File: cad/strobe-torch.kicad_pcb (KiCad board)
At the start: 2 copper layers, 81 x 34 mm, 32 parts, among them SW1 50Hz, SW2 60Hz, SW3 300Hz, U1 ATTINY25V-10SU, Y1 4.9152MHz

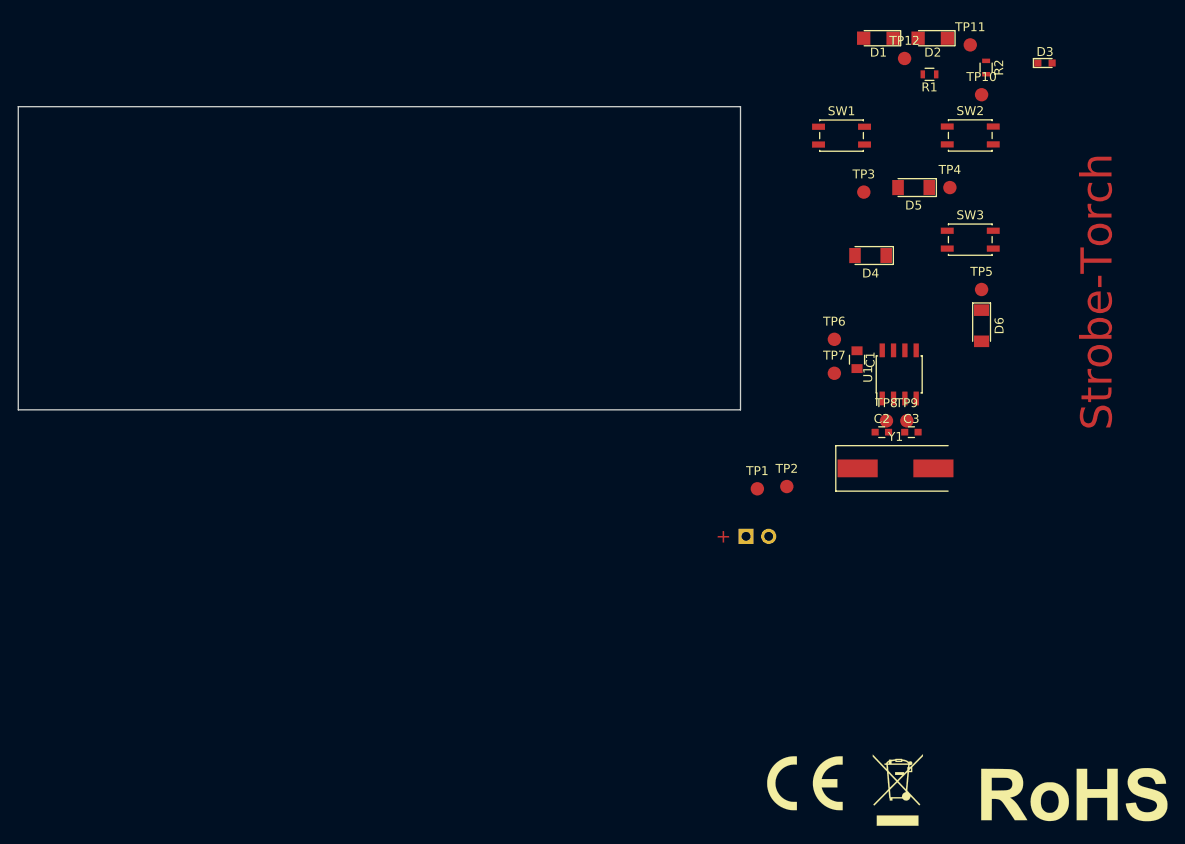
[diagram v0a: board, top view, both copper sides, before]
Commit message: Updated schematic (Output MOSFET and change to Shottky diodes, changed pinning to optimize layout)
Created footprints for Teko case and side emitting LEDs

Initial pcb layout
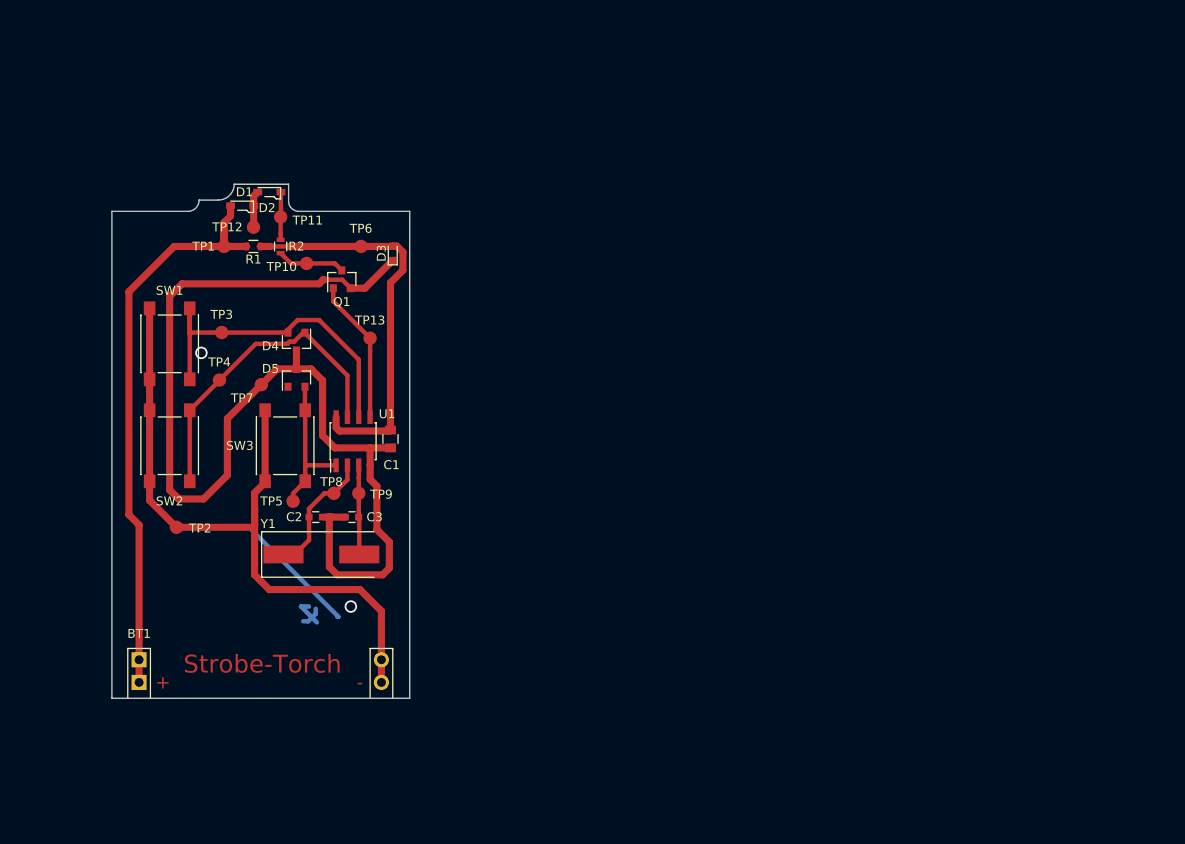
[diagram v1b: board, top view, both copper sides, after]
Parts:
- removed D6: 1N4148, Diodes_SMD:D_MiniMELF
- removed REF***: RoHS-Logo_6mm_SilkScreen, Symbols:RoHS-Logo_6mm_SilkScreen
- removed REF***: CE-Logo_8.5x6mm_SilkScreen, Symbols:CE-Logo_8.5x6mm_SilkScreen
- removed REF***: WEEE-Logo_5.6x8mm_SilkScreen, Symbols:WEEE-Logo_5.6x8mm_SilkScreen
- added Q1: BSS138, TO_SOT_Packages_SMD:SOT-23, F.Cu at (156.1, 78.4)
- added TP13: PWMout, Measurement_Points:Measurement_Point_Round-SMD-Pad_Small, F.Cu at (159.3, 85.0)
- BT1: footprint Pin_Headers:Pin_Header_Straight_1x02_Pitch2.54mm -> Battery_Holder:Teko_1112x_battery_compartment; moved to F.Cu
- D1, D2: footprint LEDs:LED_1206 -> LEDs_Side_Emitting:LED_215
- D4, D5: value 1N4148 -> BAT54A; footprint Diodes_SMD:D_MiniMELF -> TO_SOT_Packages_SMD:SOT-23
- R1: value 1k5 -> 1k8
- R2: value 270 -> 150
- SW1, SW2, SW3: footprint Buttons_Switches_SMD:SW_SPST_EVQP2 -> Buttons_Switches_SMD:SW_SPST_PTS645
- TP10: value PWMout -> Udrain
- moved SW2 96.3 mm to (136.8, 97.0), turned to 90 degrees
- moved TP4 84.7 mm to (142.4, 89.7)
- moved R2 81.6 mm to (149.2, 74.7)
- moved TP5 80.8 mm to (150.6, 103.3)
- moved SW3 80.2 mm to (149.7, 97.0), turned to 90 degrees
- moved TP11 79.7 mm to (149.2, 71.4)
- moved SW1 78.9 mm to (136.8, 85.6), turned to 90 degrees
- moved R1 78.2 mm to (146.2, 74.7)
- moved TP10 78.0 mm to (152.1, 76.6)
- moved D2 76.4 mm to (148.0, 68.6), turned to 0 degrees
- moved D3 76.2 mm to (161.8, 75.4), turned to 90 degrees
- moved TP12 75.4 mm to (146.2, 72.5)
- moved D1 73.8 mm to (144.9, 70.1), turned to 0 degrees
- moved TP3 73.7 mm to (142.6, 84.3)
- moved D5 72.4 mm to (151.0, 89.4), turned to 90 degrees
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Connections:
- D4 pad 2: GND -> Net-(D4-Pad2)
- D5 pad 1: Net-(D5-Pad1) -> (no net)
- D5 pad 2: GND -> Net-(D5-Pad2)
- R2 pad 2: Net-(R2-Pad2) -> Net-(Q1-Pad3)
- SW1 pad 2: Net-(D4-Pad1) -> Net-(D4-Pad2)
- SW2 pad 2: Net-(D5-Pad1) -> Net-(D4-Pad1)
- SW3 pad 2: Net-(D6-Pad1) -> Net-(D5-Pad2)
- TP10 pad 1: Net-(R2-Pad2) -> Net-(Q1-Pad3)
- TP3 pad 1: Net-(D4-Pad1) -> Net-(D4-Pad2)
- TP4 pad 1: Net-(D5-Pad1) -> Net-(D4-Pad1)
- TP5 pad 1: Net-(D6-Pad1) -> Net-(D5-Pad2)
- U1 pad 1: Net-(D6-Pad1) -> Net-(D5-Pad2)
- U1 pad 5: Net-(D5-Pad1) -> Net-(Q1-Pad1)
- U1 pad 6: Net-(R2-Pad2) -> Net-(D4-Pad2)
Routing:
- net GND: track 0.00 -> 124.1 mm
- net Net-(BT1-Pad2): track 0.00 -> 79.7 mm
- net +12V: track 0.00 -> 67.0 mm
- net VCC: track 0.00 -> 44.3 mm
- net Net-(D4-Pad2): track 0.00 -> 38.8 mm
- net Net-(D4-Pad1): track 0.00 -> 36.0 mm
- net (no net): track 0.00 -> 26.3 mm, vias 0 -> 2
- net Net-(D5-Pad2): track 0.00 -> 16.9 mm
- net Net-(Q1-Pad1): track 0.00 -> 16.2 mm
- net Net-(C2-Pad2): track 0.00 -> 14.3 mm
- net Net-(C3-Pad1): track 0.00 -> 10.1 mm
- net Net-(Q1-Pad3): track 0.00 -> 7.66 mm
- net Net-(D2-Pad1): track 0.00 -> 5.36 mm
- net Net-(D1-Pad1): track 0.00 -> 4.13 mm
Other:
- board size 81 x 34 mm -> 33.4 x 57.7 mm
- net class Default: trace_width 0.27 -> 0.5
- net class Led: trace_width 0.35 -> 0.8
- net class Power: trace_width 0.45 -> 0.8
- board text added: "-"

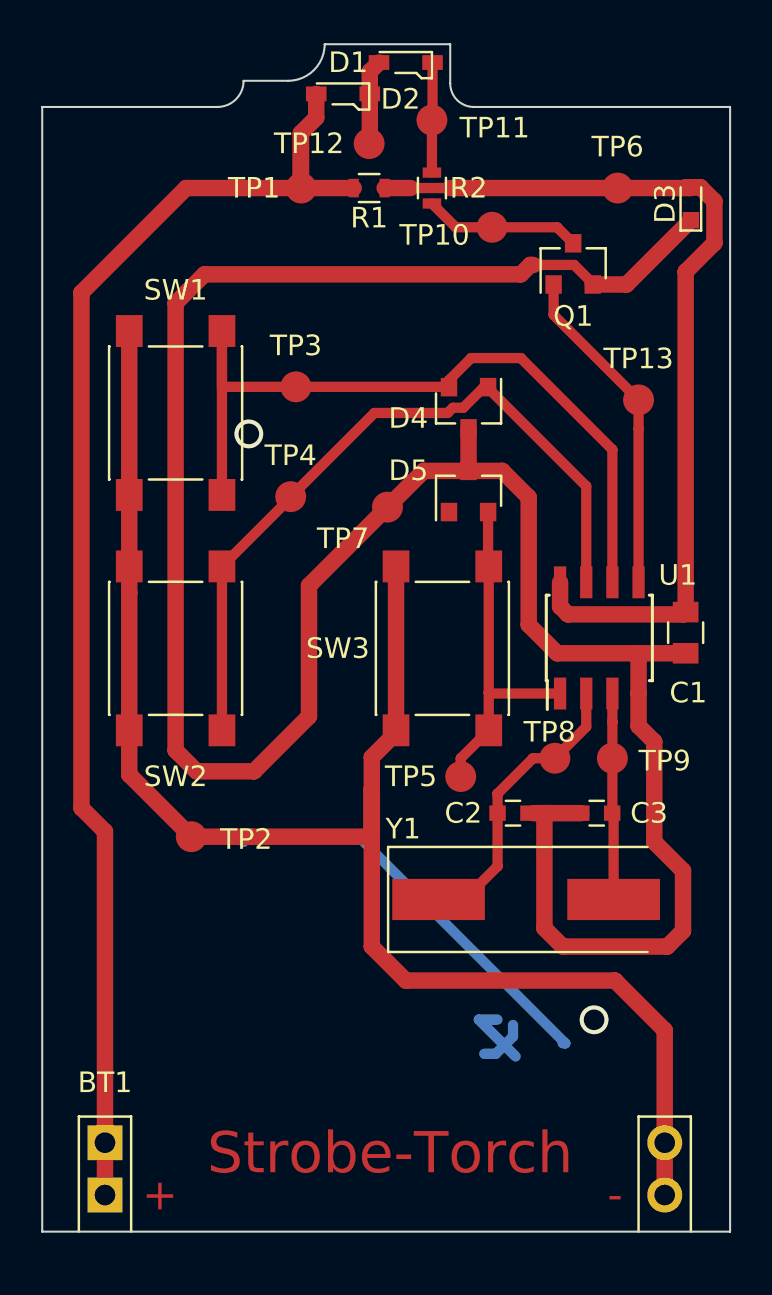
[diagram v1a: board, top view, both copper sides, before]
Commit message: Applied needed modifications after production of first samples.
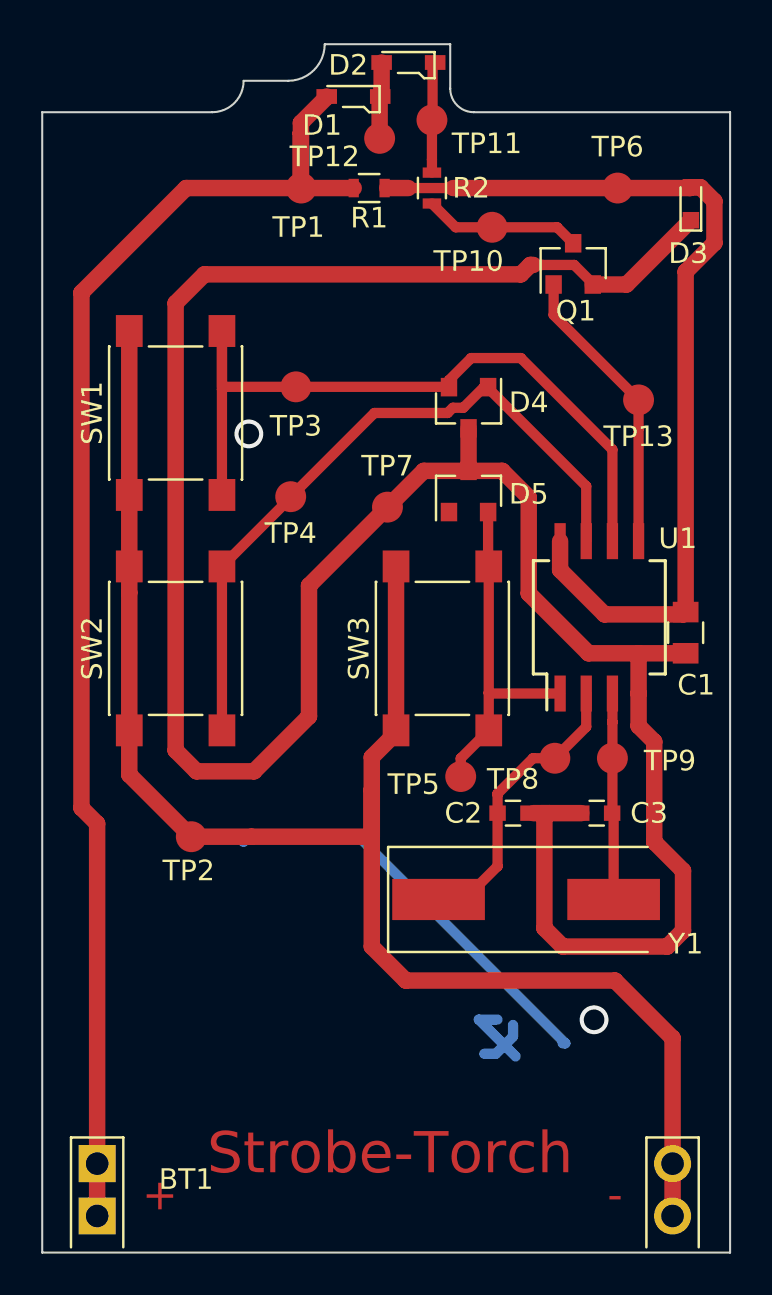
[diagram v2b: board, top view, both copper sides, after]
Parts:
- U1: footprint Housings_SOIC:SOIC-8_3.9x4.9mm_Pitch1.27mm -> Housings_SOIC:SO-8_5.3x6.2mm_Pitch1.27mm
- moved BT1 1.09 mm to (133.0, 122.0)
- moved U1 1.00 mm to (157.4, 95.5)
- moved TP12 0.57 mm to (146.7, 72.3)
- moved D1 0.52 mm to (145.4, 70.2)
- moved D2 0.13 mm to (148.1, 68.6)
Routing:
- net Net-(Q1-Pad1): track 16.2 -> 14.2 mm
- net Net-(D4-Pad2): track 38.8 -> 36.8 mm
- net Net-(D4-Pad1): track 36.0 -> 34.0 mm
- net Net-(BT1-Pad2): track 79.7 -> 80.9 mm
- net +12V: track 67.0 -> 68.0 mm
- net GND: track 124.1 -> 123.2 mm
- net VCC: track 44.3 -> 45.1 mm
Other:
- board size 33.4 x 57.7 mm -> 33.4 x 58.7 mm

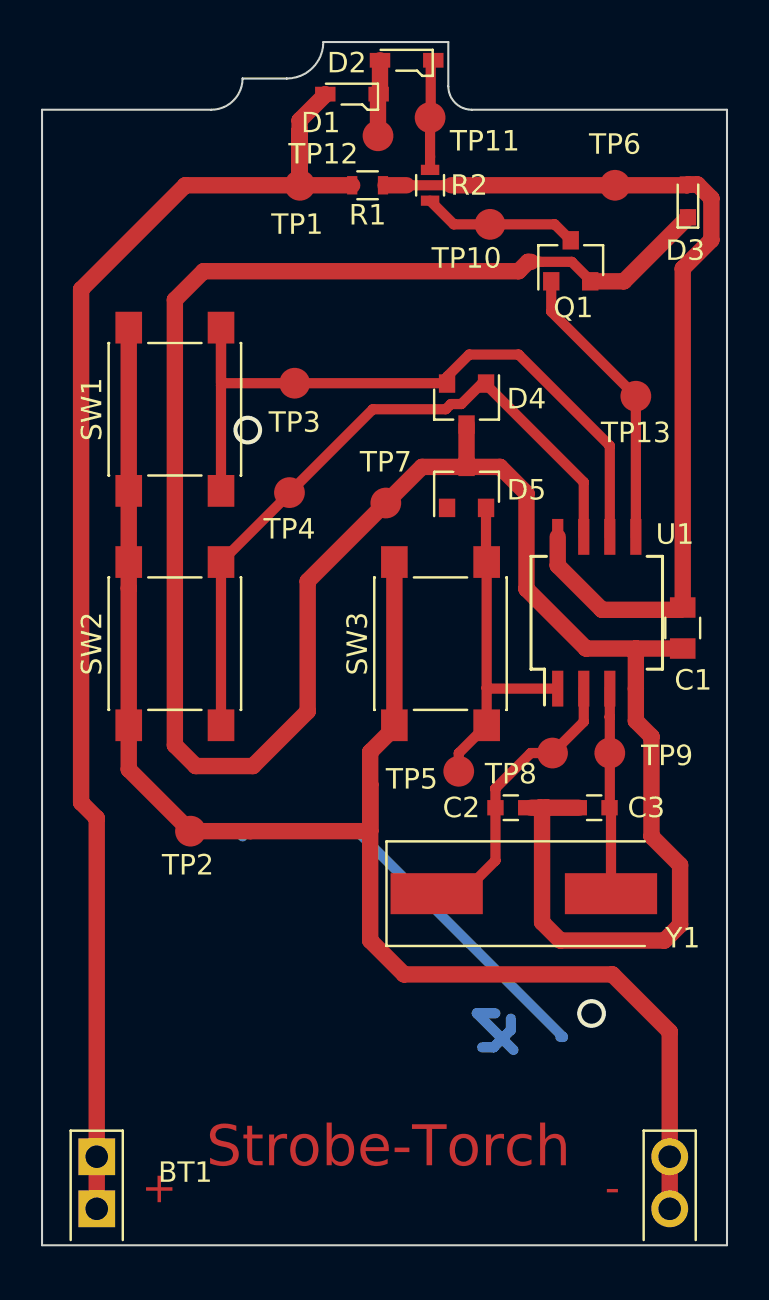
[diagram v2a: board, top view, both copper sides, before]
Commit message: Change footprint of button and upgrade to KiCad 8
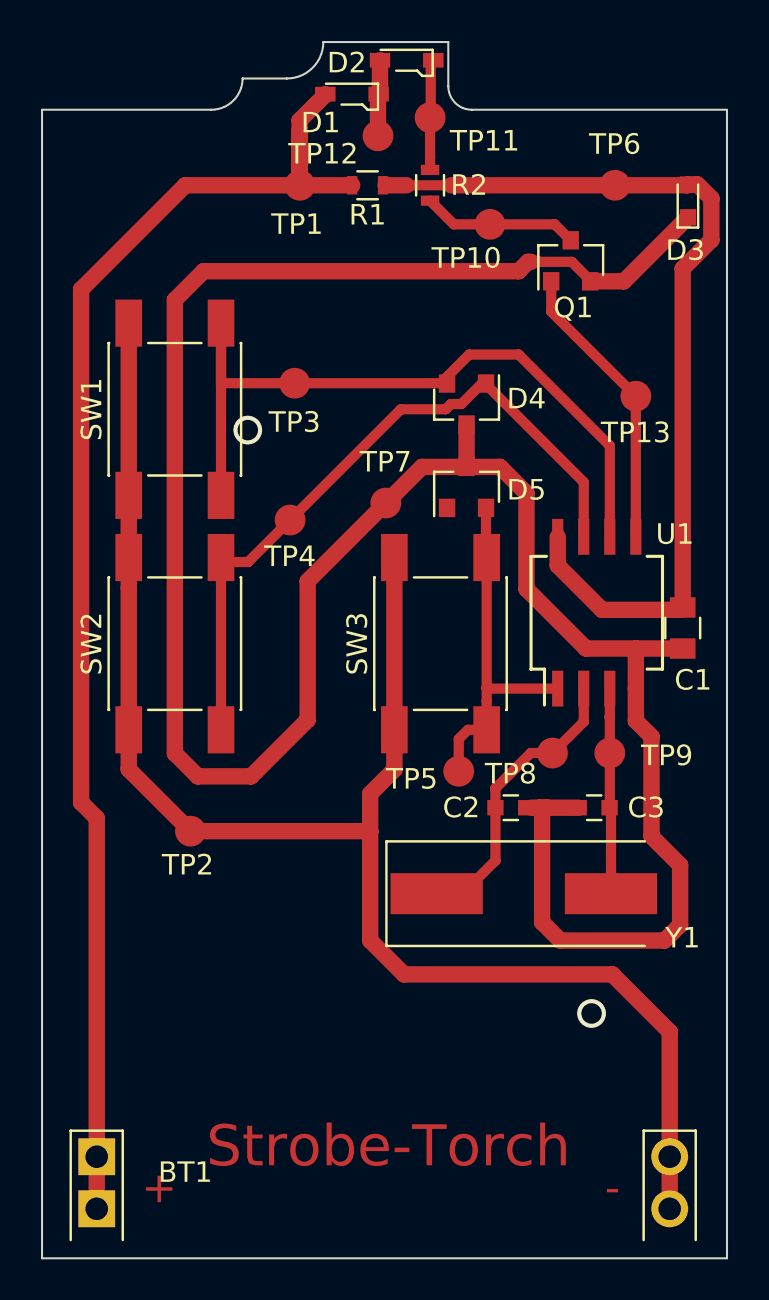
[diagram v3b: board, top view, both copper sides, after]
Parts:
- SW1: footprint Buttons_Switches_SMD:SW_SPST_PTS645 -> Button:SW_SPST_FSM6JSMA
- SW2: value 60Hz -> 300Hz; footprint Buttons_Switches_SMD:SW_SPST_PTS645 -> Button:SW_SPST_FSM6JSMA
- SW3: value 300Hz -> 60Hz; footprint Buttons_Switches_SMD:SW_SPST_PTS645 -> Button:SW_SPST_FSM6JSMA
- TP4: value 60Hz -> 300Hz
- TP5: value 300Hz -> 60Hz
- moved TP4 1.34 mm to (142.4, 91.0)
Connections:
- D5 pad 1: (no net) -> unconnected-(D5-Pad1)
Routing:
- net (no net): track 26.3 -> 0.00 mm
- net Net-(BT1--): track 80.9 -> 78.6 mm
- net GND: track 123.2 -> 124.1 mm
- net Net-(U1-PB5(~{RESET}/dW/ADC0/PCINT5)): track 16.9 -> 17.4 mm
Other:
- board size 33.4 x 58.7 mm -> 33.4 x 59.3 mm
- net class Default removed
- net class Led removed
- net class Power removed
